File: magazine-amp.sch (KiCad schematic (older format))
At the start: 39 parts

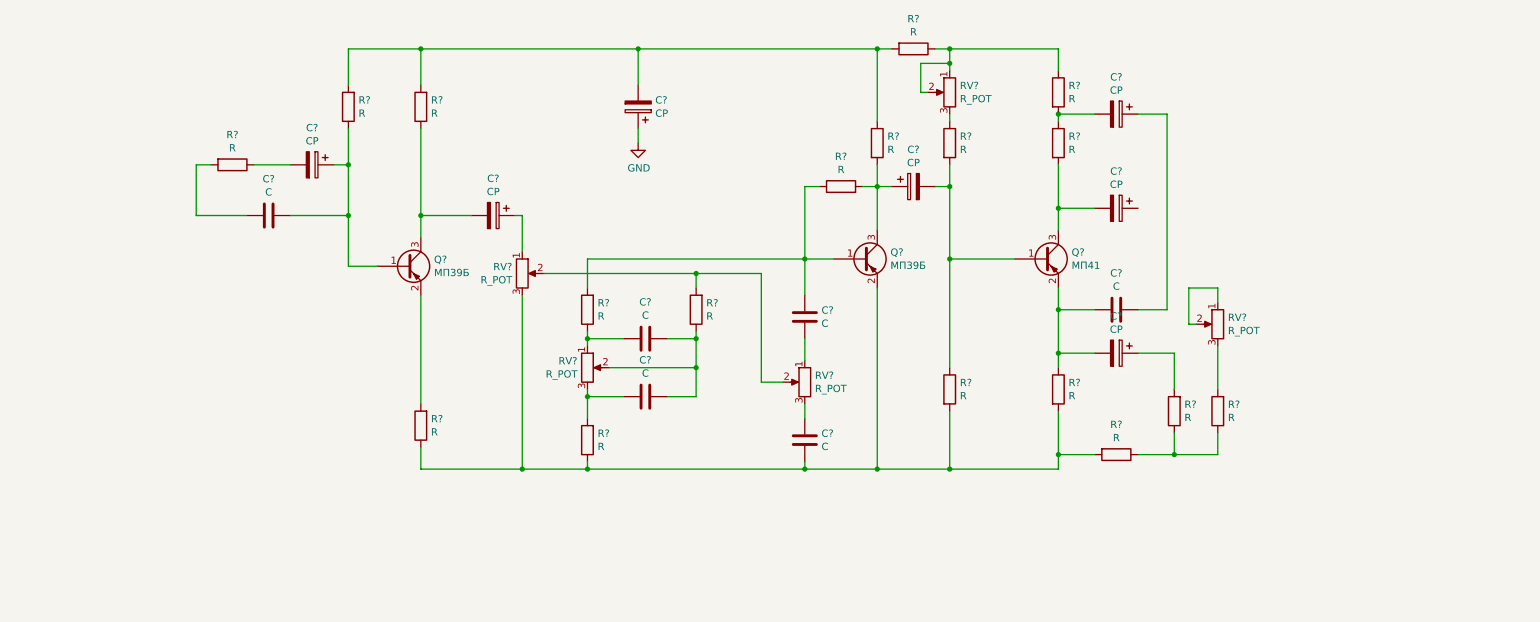
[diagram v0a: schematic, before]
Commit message: Finish top schematics
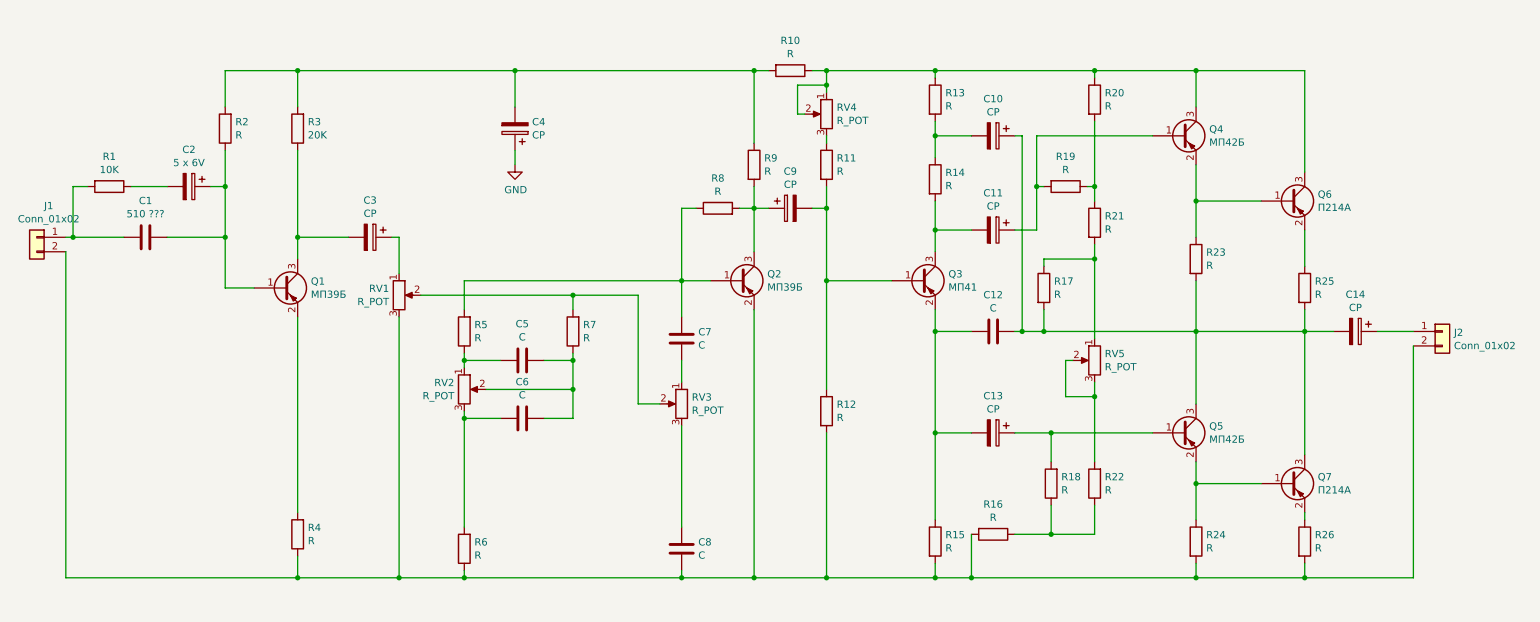
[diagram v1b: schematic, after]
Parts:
- added C14: CP, symbol Device:CP
- added J1, J2: Conn_01x02, symbol Connector_Generic:Conn_01x02
- added Q4, Q5: МП42Б, Package_TO_SOT_THT:TO-5-3, symbol components:МП42Б
- added Q6, Q7: П214А, symbol components:П214А
- added R17, R19, R20, R21, R23, R24, R25, R26: R, symbol Device:R
- C1: renamed from C?; value C -> 510 ???
- C2: renamed from C?; value CP -> 5 x 6V
- Q3: renamed from Q?; footprint (none) -> Package_TO_SOT_THT:TO-5-3
- R1: renamed from R?; value R -> 10K
- R3: renamed from R?; value R -> 20K
- gave numbers to parts that had none: 34
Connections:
- net at C1.2, R1.2: now also J1.1 (Pin_1)
- net at C8.2, Q2.2 (E), R12.2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: now also J1.2 (Pin_2), J2.2 (Pin_2), R24.2, R26.2
- net at R10.1, R13.1, RV4.1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: now also Q4.3 (C), Q6.3 (C), R20.1
- net at C10.1, C12.1: now also C14.2, Q5.3 (C), Q7.3 (C), R17.2, R23.2, R25.2
- net at C11.1: now also Q4.1 (B), R19.2
- net at C13.1, R18.2: now also Q5.1 (B)
- net at R22.2, RV5.3: now also RV5.2
- net at RV5.1: now also R17.1, R21.2; no longer RV5.2
- new net: R19.1, R20.2, R21.1
- new net: Q4.2 (E), Q6.1 (B), R23.1
- new net: Q5.2 (E), Q7.1 (B), R24.1
- new net: Q6.2 (E), R25.1
- new net: Q7.2 (E), R26.1
- new net: C14.1, J2.1 (Pin_1)
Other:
- moved on the sheet: C1, C10, C11, C12, C13, C2, C3, C4, C5, C6, C7, C8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

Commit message: Fix component values
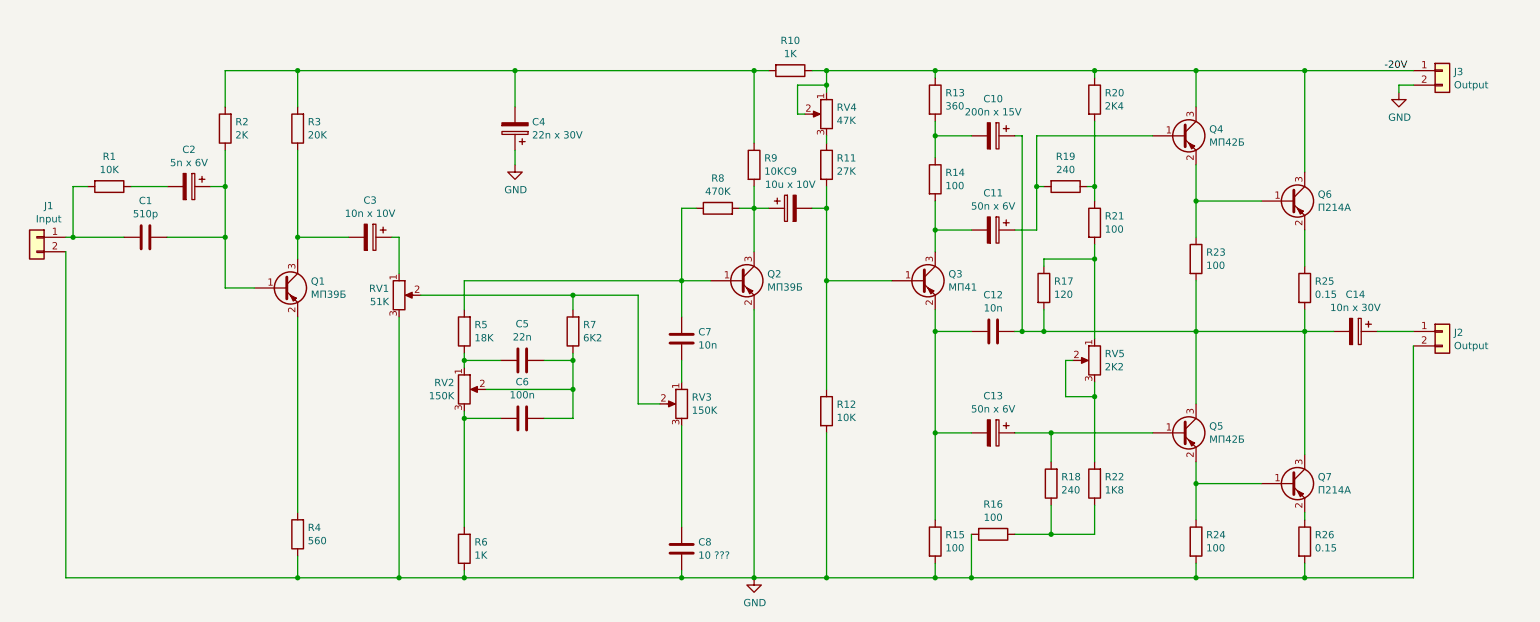
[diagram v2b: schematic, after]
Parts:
- added J3: Output, symbol Connector_Generic:Conn_01x02
- C1: value 510 ??? -> 510p
- C10: value CP -> 200n x 15V
- C11, C13: value CP -> 50n x 6V
- C12, C7: value C -> 10n
- C14: value CP -> 10n x 30V
- C2: value 5 x 6V -> 5n x 6V
- C3: value CP -> 10n x 10V
- C4: value CP -> 22n x 30V
- C5: value C -> 22n
- C6: value C -> 100n
- C8: value C -> 10 ???
- C9: value CP -> 10u x 10V
- J1: value Conn_01x02 -> Input
- J2: value Conn_01x02 -> Output
- R10, R6: value R -> 1K
- R11: value R -> 27K
- R12, R9: value R -> 10K
- R13: value R -> 360
- R14, R15, R16, R21, R23, R24: value R -> 100
- R17: value R -> 120
- R18, R19: value R -> 240
- R2: value R -> 2K
- R20: value R -> 2K4
- R22: value R -> 1K8
- R25, R26: value R -> 0.15
- R4: value R -> 560
- R5: value R -> 18K
- R7: value R -> 6K2
- R8: value R -> 470K
- RV1: value R_POT -> 51K
- RV2, RV3: value R_POT -> 150K
- RV4: value R_POT -> 47K
- RV5: value R_POT -> 2K2
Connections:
- net GND: now also C8.2, J1.2 (Pin_2), J2.2 (Pin_2), Q2.2 (E), R12.2, R15.2, R16.2, R24.2, R26.2, R4.1, R6.1, RV1.3, J3.2 (Pin_2)
- net -20V: now reaches Q4.3 (C), Q6.3 (C), R10.1, R13.1, R20.1, RV4.1, RV4.2
- net -20V: now also J3.1 (Pin_1)

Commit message: Finish schematics
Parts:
- C1, C7: footprint (none) -> Capacitor_THT:C_Disc_D4.7mm_W2.5mm_P5.00mm
- C10: value 200n x 15V -> 200u x 15V; footprint (none) -> Capacitor_THT:CP_Radial_D12.5mm_P5.00mm
- C11, C13: value 50n x 6V -> 50u x 6V; footprint (none) -> Capacitor_THT:CP_Radial_D8.0mm_P3.50mm
- C12: value 10n -> 1n; footprint (none) -> Capacitor_THT:C_Disc_D4.7mm_W2.5mm_P5.00mm
- C14: value 10n x 30V -> 1u x 30V; footprint (none) -> Capacitor_THT:CP_Radial_D8.0mm_P3.50mm
- C2: value 5n x 6V -> 5u x 6V; footprint (none) -> Capacitor_THT:CP_Radial_D4.0mm_P2.00mm
- C3: value 10n x 10V -> 10u x 10V; footprint (none) -> Capacitor_THT:CP_Radial_D7.5mm_P2.50mm
- C4: value 22n x 30V -> 22u x 30V; footprint (none) -> Capacitor_THT:CP_Radial_D10.0mm_P5.00mm
- C5: footprint (none) -> Capacitor_THT:C_Disc_D10.0mm_W2.5mm_P5.00mm
- C6: footprint (none) -> Capacitor_THT:C_Rect_L11.0mm_W3.4mm_P10.00mm_MKT
- C8: value 10 ??? -> 100n; footprint (none) -> Capacitor_THT:C_Rect_L11.0mm_W3.4mm_P10.00mm_MKT
- C9: footprint (none) -> Capacitor_THT:CP_Radial_D7.5mm_P2.50mm
- J1, J2, RV1, RV2, RV3, RV4, RV5: footprint (none) -> Connector_PinSocket_2.54mm:PinSocket_1x02_P2.54mm_Vertical
- J3: value Output -> VCC; footprint (none) -> Connector_PinSocket_2.54mm:PinSocket_1x02_P2.54mm_Vertical
- Q6, Q7: footprint (none) -> Package_TO_SOT_THT:TO-5-3
- R1, R10, R11, R12, R13, R14, R15, R16, R17, R18, R19, R2, R20, R21, R22, R23, R24, R3, R4, R5, R6, R7, R8, R9: footprint (none) -> Resistor_THT:R_Axial_DIN0414_L11.9mm_D4.5mm_P15.24mm_Horizontal
- R25, R26: footprint (none) -> Resistor_THT:R_Axial_DIN0614_L14.3mm_D5.7mm_P15.24mm_Horizontal
